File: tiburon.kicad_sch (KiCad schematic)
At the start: 1 part, among them U1 ESP32-S3-WROOM-1

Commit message: test commit
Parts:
- added Q1: IRF4905, Package_TO_SOT_THT:TO-220-3_Vertical, symbol Transistor_FET:IRF4905
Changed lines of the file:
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@@
 	(paper "A4")
+	(symbol
+		(lib_id "Transistor_FET:IRF4905")
+		(at 85.09 129.54 0)
+		(unit 1)
+		(exclude_from_sim no)
+		(in_bom yes)
+		(on_board yes)
+		(dnp no)
+		(fields_autoplaced yes)
+		(property "Reference" "Q1"
+			(at 91.44 128.2699 0)
+			(effects
+				(font
+					(size 1.27 1.27)
+				)
+				(justify left)
+			)
+		)
+		(property "Value" "IRF4905"
+			(at 91.44 130.8099 0)
+			(effects
+				(font
+					(size 1.27 1.27)
+				)
+				(justify left)
+			)
+		)
+		(property "Footprint" "Package_TO_SOT_THT:TO-220-3_Vertical"
+			(at 90.17 131.445 0)
+			(effects
+				(font
+					(size 1.27 1.27)
+					(italic yes)
+				)
+				(justify left)
+				(hide yes)
+			)
+		)
+		(property "Datasheet" "http://www.infineon.com/dgdl/irf4905.pdf?fileId=5546d462533600a4015355e32165197c"
+			(at 90.17 133.35 0)
+			(effects
+				(font
+					(size 1.27 1.27)
+				)
+				(justify left)
+				(hide yes)
+			)
+		)
+		(property "Description" "-74A Id, -55V Vds, Single P-Channel HEXFET Power MOSFET, 20mOhm Ron, TO-220AB"
+			(at 85.09 129.54 0)
+			(effects
+				(font
+					(size 1.27 1.27)
+				)
+				(hide yes)
+			)
+		)
+		(pin "2"
+		)
+		(pin "3"
+		)
+		(pin "1"
+		)
+		(instances
+			(project ""
+				(path "/6d12a6c8-8052-4e19-9b4d-c9c58cadbdb7"
+					(reference "Q1")
+					(unit 1)
+				)
+			)
+		)
+	)
 	(symbol
 		(lib_id "RF_Module:ESP32-S3-WROOM-1")

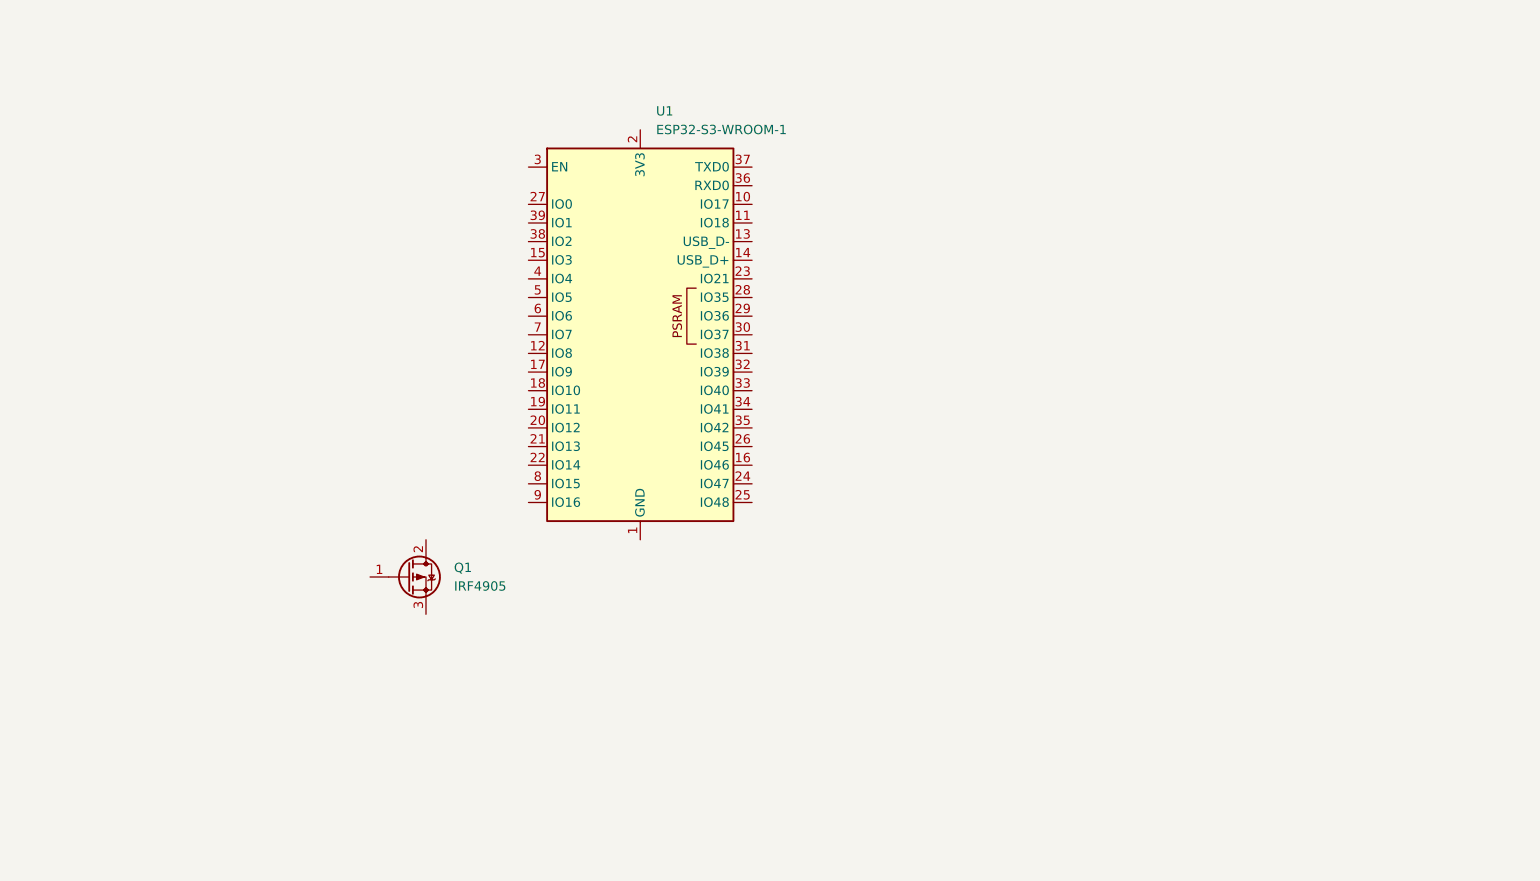
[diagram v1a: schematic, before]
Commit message: I2C and SD Card Connections
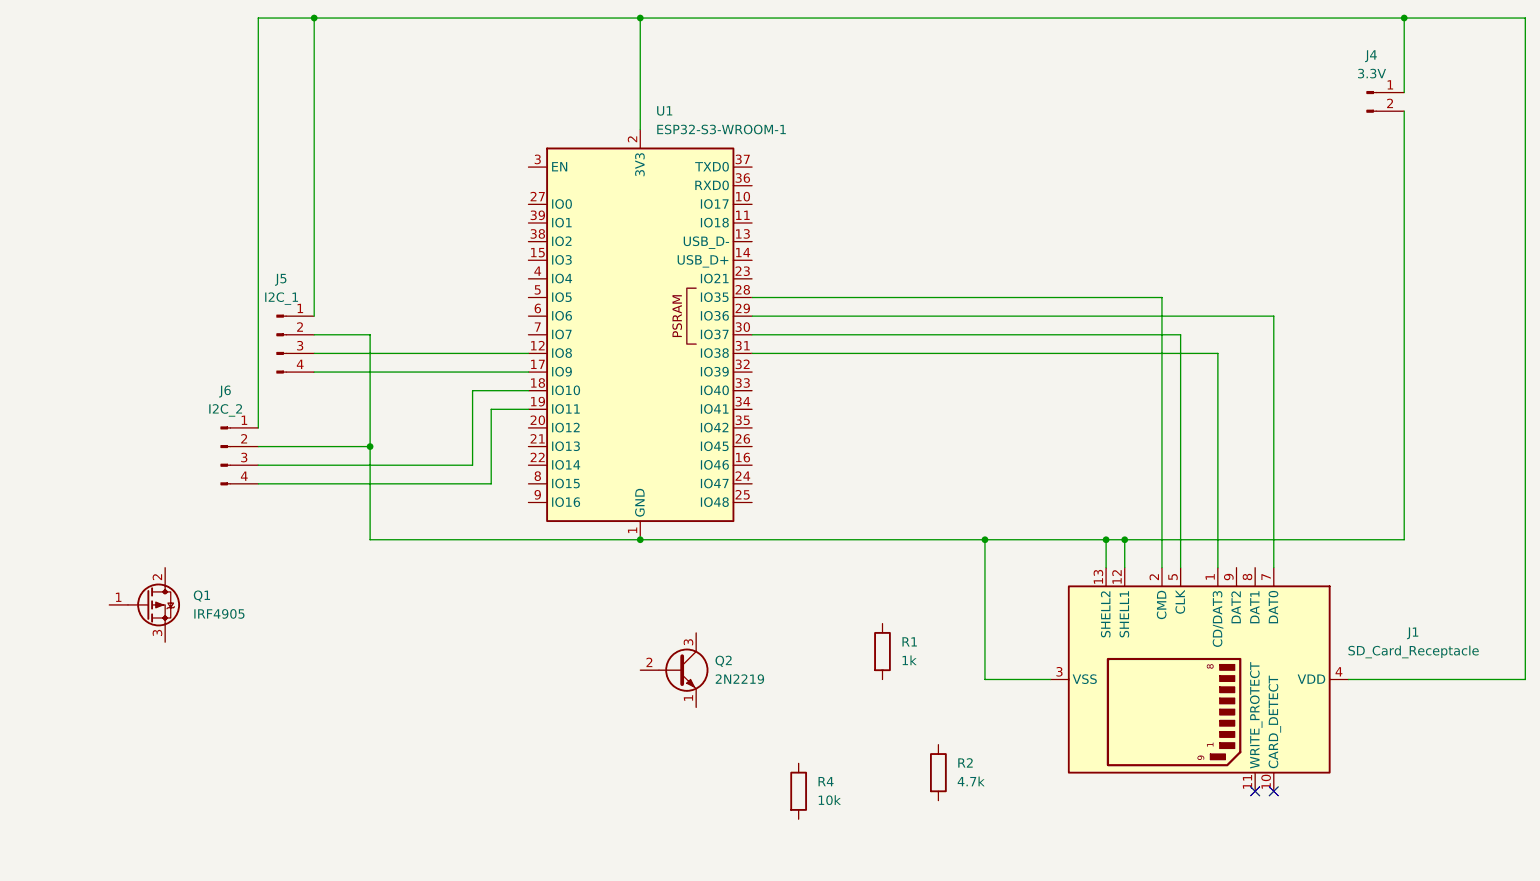
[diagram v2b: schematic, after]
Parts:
- added J1: SD_Card_Receptacle, symbol Connector:SD_Card_Receptacle
- added J4: 3.3V, symbol Connector:Conn_01x02_Pin
- added J5: I2C_1, symbol Connector:Conn_01x04_Pin
- added J6: I2C_2, symbol Connector:Conn_01x04_Pin
- added Q2: 2N2219, Package_TO_SOT_THT:TO-39-3, symbol Transistor_BJT:2N2219
- added R1: 1k, symbol Device:R
- added R2: 4.7k, symbol Device:R
- added R4: 10k, symbol Device:R
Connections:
- net at U1.1 (GND), U1.40 (GND), U1.41 (GND): now also J1.12 (SHELL1), J1.13 (SHELL2), J1.3 (VSS), J1.6 (VSS), J4.2 (Pin_2), J5.2 (Pin_2), J6.2 (Pin_2)
- net at U1.12 (IO8): now also J5.3 (Pin_3)
- net at U1.17 (IO9): now also J5.4 (Pin_4)
- net at U1.18 (IO10): now also J6.3 (Pin_3)
- net at U1.19 (IO11): now also J6.4 (Pin_4)
- net at U1.2 (3V3): now also J1.4 (VDD), J4.1 (Pin_1), J5.1 (Pin_1), J6.1 (Pin_1)
- net at U1.28 (IO35): now also J1.2 (CMD)
- net at U1.29 (IO36): now also J1.7 (DAT0)
- net at U1.30 (IO37): now also J1.5 (CLK)
- net at U1.31 (IO38): now also J1.1 (CD/DAT3)
- no-connect marks 0 -> 2
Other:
- moved on the sheet: Q1

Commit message: cleaned circuit, added thruster
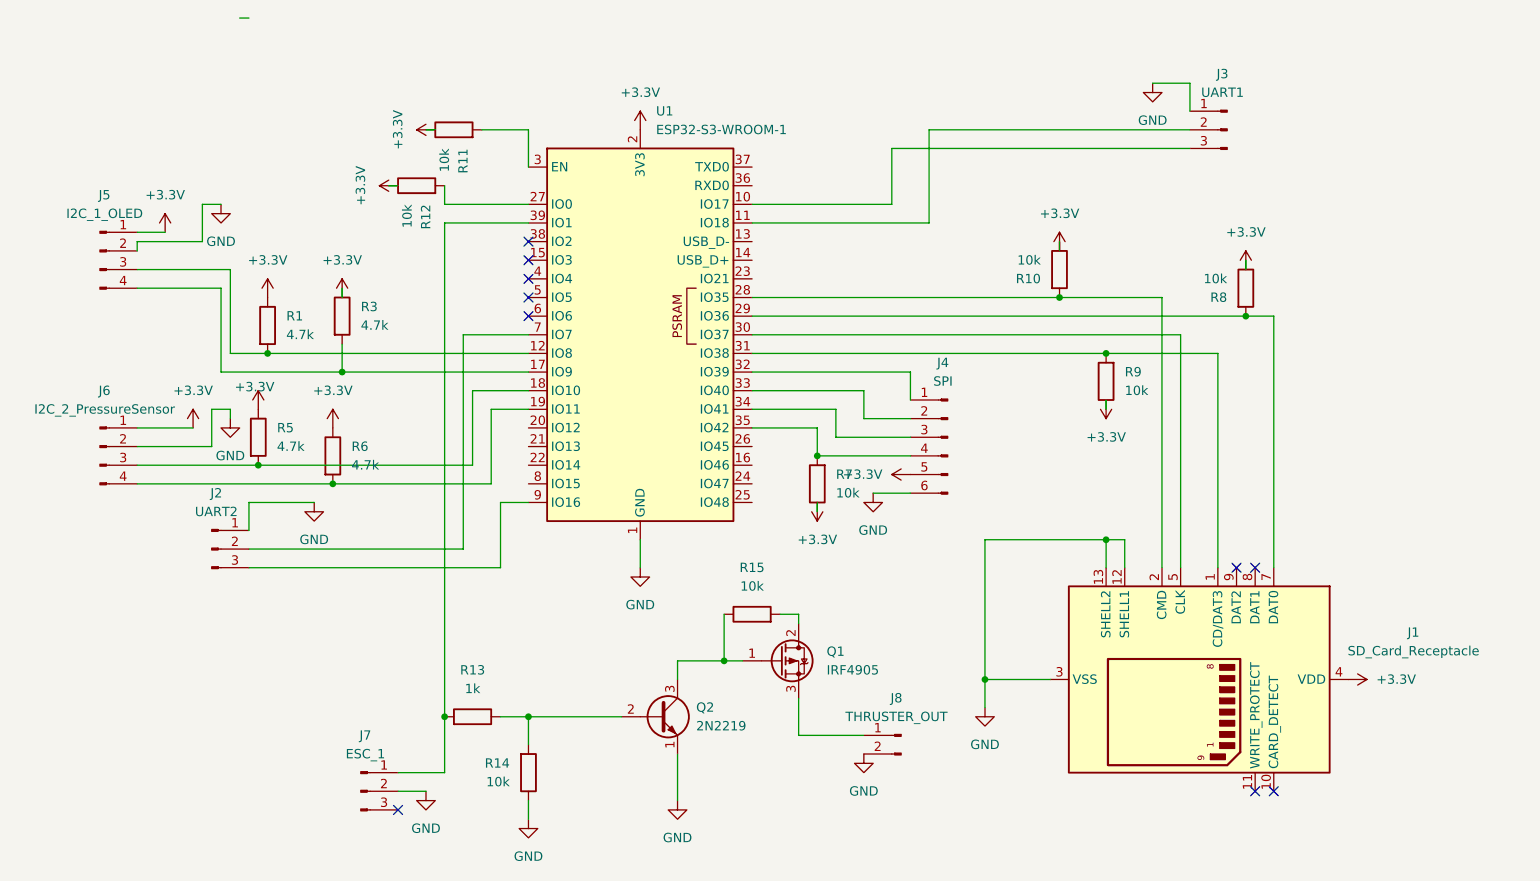
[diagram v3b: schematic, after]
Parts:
- removed J4: 3.3V, symbol Connector:Conn_01x02_Pin
- removed R2: 4.7k, symbol Device:R
- removed R4: 10k, symbol Device:R
- added J2: UART2, symbol Connector:Conn_01x03_Pin
- added J3: UART1, symbol Connector:Conn_01x03_Pin
- added J4: SPI, symbol Connector:Conn_01x06_Pin
- added J7: ESC_1, symbol Connector:Conn_01x03_Pin
- added J8: THRUSTER_OUT, symbol Connector:Conn_01x02_Pin
- added R10, R11, R12, R14, R15, R7, R8, R9: 10k, symbol Device:R
- added R13: 1k, symbol Device:R
- added R3, R5, R6: 4.7k, symbol Device:R
- J5: value I2C_1 -> I2C_1_OLED
- J6: value I2C_2 -> I2C_2_PressureSensor
- R1: value 1k -> 4.7k
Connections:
- net at Q1.1 (G): now also Q2.3 (C), R15.1
- net at Q1.2 (D): now also R15.2
- net at Q1.3 (S): now also J8.1 (Pin_1)
- net GND: now reaches Q2.1 (E)
- net GND: now also J1.12 (SHELL1), J1.13 (SHELL2), J1.3 (VSS), J1.6 (VSS), J5.2 (Pin_2), J6.2 (Pin_2), U1.1 (GND), U1.40 (GND), U1.41 (GND), J2.1 (Pin_1), J3.1 (Pin_1), J4.6 (Pin_6), J7.2 (Pin_2), J8.2 (Pin_2), R14.1
- net at Q2.2 (B): now also R13.1, R14.2
- net +3.3V: now reaches J1.4 (VDD), J5.1 (Pin_1), J6.1 (Pin_1), U1.2 (3V3)
- net +3.3V: now also R1.1, J4.5 (Pin_5), R10.1, R11.1, R12.1, R3.1, R5.1, R6.1, R7.1, R8.1, R9.1
- net at J6.3 (Pin_3), U1.18 (IO10): now also R5.2
- net at J6.4 (Pin_4), U1.19 (IO11): now also R6.2
- net at U1.10 (IO17): now also J3.3 (Pin_3)
- net at U1.11 (IO18): now also J3.2 (Pin_2)
- net at J5.3 (Pin_3), U1.12 (IO8): now also R1.2
- net at J5.4 (Pin_4), U1.17 (IO9): now also R3.2
- net at U1.27 (IO0): now also R12.2
- net at J1.2 (CMD), U1.28 (IO35): now also R10.2
- net at J1.7 (DAT0), U1.29 (IO36): now also R8.2
- net at U1.3 (EN): now also R11.2
- net at J1.1 (CD/DAT3), U1.31 (IO38): now also R9.2
- net at U1.32 (IO39): now also J4.1 (Pin_1)
- net at U1.33 (IO40): now also J4.2 (Pin_2)
- net at U1.34 (IO41): now also J4.3 (Pin_3)
- net at U1.35 (IO42): now also J4.4 (Pin_4), R7.2
- net at U1.39 (IO1): now also J7.1 (Pin_1), R13.2
- net at U1.7 (IO7): now also J2.2 (Pin_2)
- net at U1.9 (IO16): now also J2.3 (Pin_3)
- no-connect marks 2 -> 10
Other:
- moved on the sheet: J5, J6, Q1, Q2

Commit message: fixed thruster circuit
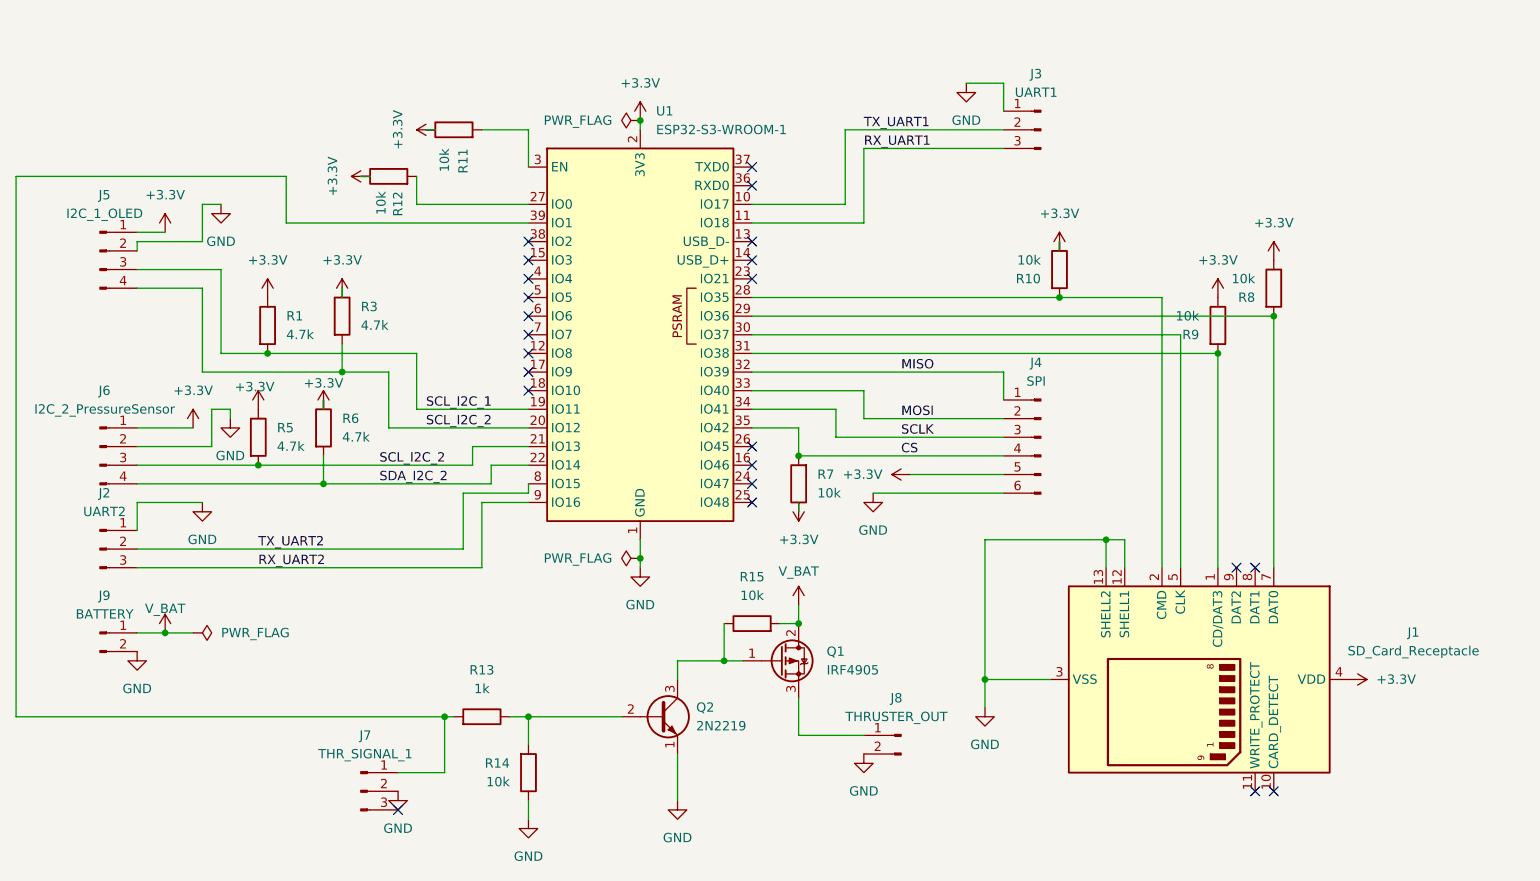
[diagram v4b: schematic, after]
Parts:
- added J9: BATTERY, symbol Connector:Conn_01x02_Pin
- J7: value ESC_1 -> THR_SIGNAL_1
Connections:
- net GND: now also J9.2 (Pin_2)
- net V_BAT: now reaches Q1.2 (D), R15.2
- net V_BAT: now also J9.1 (Pin_1)
- net at U1.7 (IO7): no longer J2.2 (Pin_2)
- net RX_UART2: now reaches J2.3 (Pin_3), U1.9 (IO16)
- net SDA_I2C_2: now reaches J6.4 (Pin_4), R6.2
- net SDA_I2C_2: now also U1.22 (IO14); no longer U1.19 (IO11)
- net SCL_I2C_2: now reaches J6.3 (Pin_3), R5.2
- net SCL_I2C_2: now also J5.4 (Pin_4), R3.2, U1.20 (IO12), U1.21 (IO13); no longer U1.18 (IO10)
- net RX_UART1: now reaches U1.11 (IO18)
- net RX_UART1: now also J3.3 (Pin_3); no longer J3.2 (Pin_2)
- net TX_UART1: now reaches U1.10 (IO17)
- net TX_UART1: now also J3.2 (Pin_2); no longer J3.3 (Pin_3)
- net SCL_I2C_1: now reaches J5.3 (Pin_3), R1.2
- net SCL_I2C_1: now also U1.19 (IO11); no longer U1.12 (IO8)
- net CS: now reaches J4.4 (Pin_4), R7.2, U1.35 (IO42)
- net MISO: now reaches J4.1 (Pin_1), U1.32 (IO39)
- net MOSI: now reaches J4.2 (Pin_2), U1.33 (IO40)
- net SCLK: now reaches J4.3 (Pin_3), U1.34 (IO41)
- net TX_UART2: now reaches U1.8 (IO15)
- net TX_UART2: now also J2.2 (Pin_2)
- now unconnected: U1.17 (IO9)
- no-connect marks 10 -> 23
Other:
- moved on the sheet: J2, J3, J4, R12, R13, R15, R6, R7, R8, R9
